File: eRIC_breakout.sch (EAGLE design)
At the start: 7 parts, among them U1 ERIC

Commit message: v1.6 ordered 4/18/2015
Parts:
- H1, H2: value M121X12_NO_SILK_KIT -> (none); device SparkFun-Connectors:M121X12_NO_SILK_KIT -> adafruit:PINHD-1X12-CB
- renumbered U1 to IC1
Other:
- moved on the sheet: H1, H2

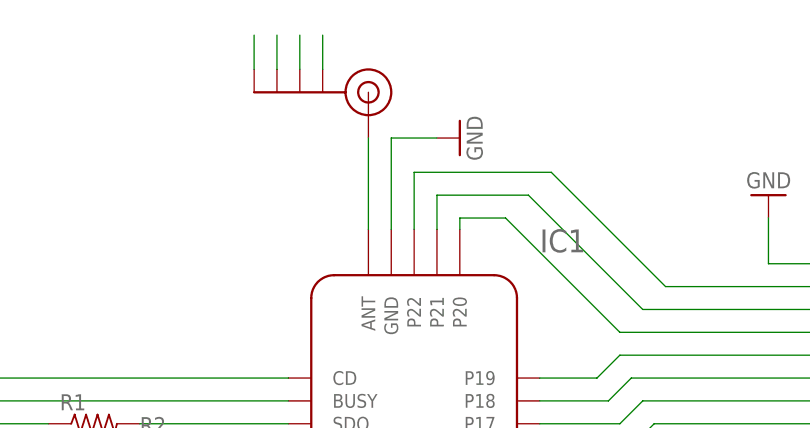
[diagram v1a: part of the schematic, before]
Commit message: SMA GND schematic changes and IC name added
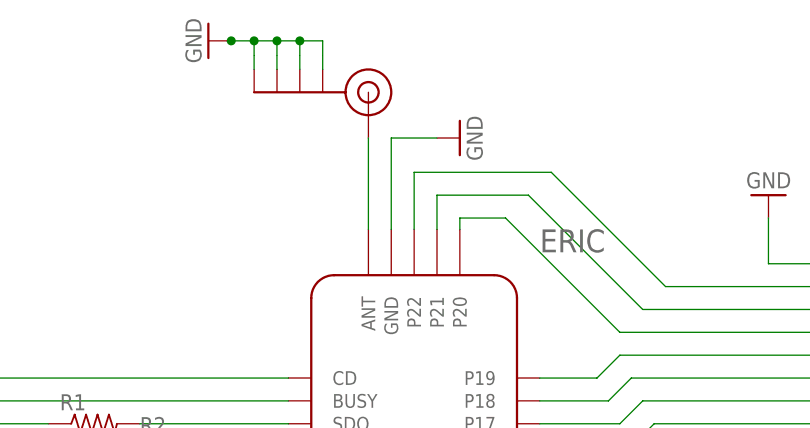
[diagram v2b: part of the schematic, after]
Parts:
- renumbered IC1 to ERIC
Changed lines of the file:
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@@
 </classes>
 <parts>
-<part name="IC1" library="lprs" deviceset="ERIC" device=""/>
+<part name="ERIC" library="lprs" deviceset="ERIC" device=""/>
 <part name="H2" library="adafruit" deviceset="PINHD-1X12" device="-CB"/>
 <part name="H1" library="adafruit" deviceset="PINHD-1X12" device="-CB"/>
@@
 <part name="J$1" library="SparkFun-Connectors" deviceset="SMA_EDGE" device=""/>
 <part name="GND1" library="supply1" deviceset="GND" device=""/>
+<part name="GND4" library="supply1" deviceset="GND" device=""/>
 </parts>
 <sheets>
@@
 </plain>
 <instances>
-<instance part="IC1" gate="G$1" x="38.1" y="34.29"/>
+<instance part="ERIC" gate="G$1" x="38.1" y="34.29"/>
 <instance part="H2" gate="G$1" x="105.41" y="55.88"/>
 <instance part="H1" gate="G$1" x="-5.08" y="43.18" rot="MR0"/>
@@
 <instance part="J$1" gate="1" x="46.99" y="87.63" rot="R270"/>
 <instance part="GND1" gate="1" x="91.44" y="76.2" rot="R180"/>
+<instance part="GND4" gate="1" x="29.21" y="93.345" rot="R270"/>
 </instances>
 <busses>
@@
 <segment>
 <pinref part="H1" gate="G$1" pin="1"/>
-<pinref part="IC1" gate="G$1" pin="CD"/>
+<pinref part="ERIC" gate="G$1" pin="CD"/>
 <wire x1="-2.54" y1="55.88" x2="38.1" y2="55.88" width="0.1524" layer="91"/>
 </segment>
@@
 <segment>
 <pinref part="H1" gate="G$1" pin="2"/>
-<pinref part="IC1" gate="G$1" pin="BUSY"/>
+<pinref part="ERIC" gate="G$1" pin="BUSY"/>
 <wire x1="-2.54" y1="53.34" x2="38.1" y2="53.34" width="0.1524" layer="91"/>
 </segment>
@@
 <segment>
 <pinref part="J$1" gate="1" pin="SIGNAL"/>
-<pinref part="IC1" gate="G$1" pin="ANT"/>
+<pinref part="ERIC" gate="G$1" pin="ANT"/>
 <wire x1="46.99" y1="82.55" x2="46.99" y2="72.39" width="0.1524" layer="91"/>
 </segment>
@@
 <segment>
 <pinref part="R1" gate="G$1" pin="2"/>
-<pinref part="IC1" gate="G$1" pin="SDO"/>
+<pinref part="ERIC" gate="G$1" pin="SDO"/>
 <wire x1="21.59" y1="50.8" x2="38.1" y2="50.8" width="0.1524" layer="91"/>
 </segment>
@@
 </segment>
 <segment>
-<pinref part="IC1" gate="G$1" pin="SDI"/>
+<pinref part="ERIC" gate="G$1" pin="SDI"/>
 <pinref part="R2" gate="G$1" pin="2"/>
 <wire x1="38.1" y1="48.26" x2="30.48" y2="48.26" width="0.1524" layer="91"/>
@@
 <segment>
 <pinref part="H1" gate="G$1" pin="5"/>
-<pinref part="IC1" gate="G$1" pin="HR"/>
+<pinref part="ERIC" gate="G$1" pin="HR"/>
 <wire x1="-2.54" y1="45.72" x2="38.1" y2="45.72" width="0.1524" layer="91"/>
 </segment>
@@
 <segment>
 <pinref part="H1" gate="G$1" pin="6"/>
-<pinref part="IC1" gate="G$1" pin="VCC"/>
+<pinref part="ERIC" gate="G$1" pin="VCC"/>
 <wire x1="-2.54" y1="43.18" x2="24.13" y2="43.18" width="0.1524" layer="91"/>
 <pinref part="C1" gate="G$1" pin="2"/>
@@
 <segment>
 <pinref part="H1" gate="G$1" pin="8"/>
-<pinref part="IC1" gate="G$1" pin="P8"/>
+<pinref part="ERIC" gate="G$1" pin="P8"/>
 <wire x1="-2.54" y1="38.1" x2="12.7" y2="38.1" width="0.1524" layer="91"/>
 <wire x1="12.7" y1="38.1" x2="29.21" y2="21.59" width="0.1524" layer="91"/>
@@
 <net name="N$12" class="0">
 <segment>
-<pinref part="IC1" gate="G$1" pin="RST"/>
+<pinref part="ERIC" gate="G$1" pin="RST"/>
 <pinref part="H1" gate="G$1" pin="9"/>
 <wire x1="49.53" y1="24.13" x2="49.53" y2="19.05" width="0.1524" layer="91"/>
@@
 <segment>
 <pinref part="H1" gate="G$1" pin="10"/>
-<pinref part="IC1" gate="G$1" pin="P10"/>
+<pinref part="ERIC" gate="G$1" pin="P10"/>
 <wire x1="-2.54" y1="33.02" x2="12.7" y2="33.02" width="0.1524" layer="91"/>
 <wire x1="12.7" y1="33.02" x2="29.21" y2="16.51" width="0.1524" layer="91"/>
@@
 <net name="N$14" class="0">
 <segment>
-<pinref part="IC1" gate="G$1" pin="P11"/>
+<pinref part="ERIC" gate="G$1" pin="P11"/>
 <pinref part="H1" gate="G$1" pin="11"/>
 <wire x1="54.61" y1="24.13" x2="54.61" y2="13.97" width="0.1524" layer="91"/>
@@
 <segment>
 <pinref part="H1" gate="G$1" pin="12"/>
-<pinref part="IC1" gate="G$1" pin="P12"/>
+<pinref part="ERIC" gate="G$1" pin="P12"/>
 <wire x1="-2.54" y1="27.94" x2="12.7" y2="27.94" width="0.1524" layer="91"/>
 <wire x1="12.7" y1="27.94" x2="29.21" y2="11.43" width="0.1524" layer="91"/>
@@
 <segment>
 <pinref part="GND2" gate="1" pin="GND"/>
-<pinref part="IC1" gate="G$1" pin="GND@2"/>
+<pinref part="ERIC" gate="G$1" pin="GND@2"/>
 <wire x1="54.61" y1="82.55" x2="49.53" y2="82.55" width="0.1524" layer="91"/>
 <wire x1="49.53" y1="82.55" x2="49.53" y2="72.39" width="0.1524" layer="91"/>
@@
 <segment>
 <pinref part="C1" gate="G$1" pin="1"/>
-<pinref part="IC1" gate="G$1" pin="GND@1"/>
+<pinref part="ERIC" gate="G$1" pin="GND@1"/>
 <wire x1="24.13" y1="35.56" x2="27.94" y2="35.56" width="0.1524" layer="91"/>
 <wire x1="27.94" y1="35.56" x2="33.02" y2="40.64" width="0.1524" layer="91"/>
@@
 <segment>
 <pinref part="J$1" gate="1" pin="GND@3"/>
-<wire x1="34.29" y1="90.17" x2="34.29" y2="93.98" width="0.1524" layer="91"/>
+<wire x1="34.29" y1="90.17" x2="34.29" y2="91.694" width="0.1524" layer="91"/>
 </segment>
 <segment>
 <pinref part="J$1" gate="1" pin="GND@2"/>
-<wire x1="36.83" y1="90.17" x2="36.83" y2="93.98" width="0.1524" layer="91"/>
+<wire x1="36.83" y1="90.17" x2="36.83" y2="91.694" width="0.1524" layer="91"/>
 </segment>
 <segment>
 <pinref part="J$1" gate="1" pin="GND@1"/>
-<wire x1="39.37" y1="90.17" x2="39.37" y2="93.98" width="0.1524" layer="91"/>
+<wire x1="39.37" y1="90.17" x2="39.37" y2="91.694" width="0.1524" layer="91"/>
 </segment>
 <segment>
 <pinref part="J$1" gate="1" pin="GND@0"/>
-<wire x1="41.91" y1="90.17" x2="41.91" y2="93.98" width="0.1524" layer="91"/>
+<wire x1="41.91" y1="90.17" x2="41.91" y2="91.694" width="0.1524" layer="91"/>
+</segment>
+<segment>
+<wire x1="34.29" y1="91.7575" x2="34.29" y2="93.345" width="0.1524" layer="91"/>
+<wire x1="34.29" y1="93.345" x2="31.75" y2="93.345" width="0.1524" layer="91"/>
+<wire x1="31.75" y1="93.345" x2="31.623" y2="93.345" width="0.1524" layer="91"/>
+<wire x1="36.83" y1="91.7575" x2="36.83" y2="93.345" width="0.1524" layer="91"/>
+<wire x1="36.83" y1="93.345" x2="34.29" y2="93.345" width="0.1524" layer="91"/>
+<junction x="34.29" y="93.345"/>
+<wire x1="39.37" y1="91.7575" x2="39.37" y2="93.345" width="0.1524" layer="91"/>
+<wire x1="39.37" y1="93.345" x2="36.83" y2="93.345" width="0.1524" layer="91"/>
+<junction x="36.83" y="93.345"/>
+<wire x1="41.91" y1="91.7575" x2="41.91" y2="93.345" width="0.1524" layer="91"/>
+<wire x1="41.91" y1="93.345" x2="39.37" y2="93.345" width="0.1524" layer="91"/>
+<junction x="39.37" y="93.345"/>
+<pinref part="GND4" gate="1" pin="GND"/>
+<junction x="31.75" y="93.345"/>
 </segment>
 </net>
 <net name="N$24" class="0">
 <segment>
-<pinref part="IC1" gate="G$1" pin="FS"/>
+<pinref part="ERIC" gate="G$1" pin="FS"/>
 <pinref part="H2" gate="G$1" pin="11"/>
 <wire x1="66.04" y1="43.18" x2="102.87" y2="43.18" width="0.1524" layer="91"/>
@@
 <net name="N$25" class="0">
 <segment>
-<pinref part="IC1" gate="G$1" pin="P13"/>
+<pinref part="ERIC" gate="G$1" pin="P13"/>
 <pinref part="H2" gate="G$1" pin="10"/>
 <wire x1="66.04" y1="40.64" x2="85.09" y2="40.64" width="0.1524" layer="91"/>
@@
 <net name="N$16" class="0">
 <segment>
-<pinref part="IC1" gate="G$1" pin="P15"/>
+<pinref part="ERIC" gate="G$1" pin="P15"/>
 <pinref part="H2" gate="G$1" pin="9"/>
 <wire x1="66.04" y1="45.72" x2="77.47" y2="45.72" width="0.1524" layer="91"/>
@@
 <segment>
 <pinref part="H2" gate="G$1" pin="8"/>
-<pinref part="IC1" gate="G$1" pin="P16"/>
+<pinref part="ERIC" gate="G$1" pin="P16"/>
 <wire x1="102.87" y1="50.8" x2="78.74" y2="50.8" width="0.1524" layer="91"/>
 <wire x1="78.74" y1="50.8" x2="76.2" y2="48.26" width="0.1524" layer="91"/>
@@
 <net name="N$18" class="0">
 <segment>
-<pinref part="IC1" gate="G$1" pin="P17"/>
+<pinref part="ERIC" gate="G$1" pin="P17"/>
 <pinref part="H2" gate="G$1" pin="7"/>
 <wire x1="66.04" y1="50.8" x2="74.93" y2="50.8" width="0.1524" layer="91"/>
@@
 <segment>
 <pinref part="H2" gate="G$1" pin="6"/>
-<pinref part="IC1" gate="G$1" pin="P18"/>
+<pinref part="ERIC" gate="G$1" pin="P18"/>
 <wire x1="102.87" y1="55.88" x2="76.2" y2="55.88" width="0.1524" layer="91"/>
 <wire x1="76.2" y1="55.88" x2="73.66" y2="53.34" width="0.1524" layer="91"/>
@@
 <net name="N$20" class="0">
 <segment>
-<pinref part="IC1" gate="G$1" pin="P19"/>
+<pinref part="ERIC" gate="G$1" pin="P19"/>
 <pinref part="H2" gate="G$1" pin="5"/>
 <wire x1="66.04" y1="55.88" x2="72.39" y2="55.88" width="0.1524" layer="91"/>
@@
 <segment>
 <pinref part="H2" gate="G$1" pin="4"/>
-<pinref part="IC1" gate="G$1" pin="P20"/>
+<pinref part="ERIC" gate="G$1" pin="P20"/>
 <wire x1="102.87" y1="60.96" x2="74.93" y2="60.96" width="0.1524" layer="91"/>
 <wire x1="74.93" y1="60.96" x2="62.23" y2="73.66" width="0.1524" layer="91"/>
@@
 <net name="N$22" class="0">
 <segment>
-<pinref part="IC1" gate="G$1" pin="P21"/>
+<pinref part="ERIC" gate="G$1" pin="P21"/>
 <pinref part="H2" gate="G$1" pin="3"/>
 <wire x1="54.61" y1="72.39" x2="54.61" y2="76.2" width="0.1524" layer="91"/>
@@
 <net name="N$23" class="0">
 <segment>
-<pinref part="IC1" gate="G$1" pin="P22"/>
+<pinref part="ERIC" gate="G$1" pin="P22"/>
 <pinref part="H2" gate="G$1" pin="2"/>
 <wire x1="52.07" y1="72.39" x2="52.07" y2="78.74" width="0.1524" layer="91"/>

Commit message: component values
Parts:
- C1: value (none) -> .1uF
- R1, R2: value (none) -> 10K
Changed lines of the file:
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@@
 <setting verticaltext="up"/>
 </settings>
-<grid distance="0.0635" unitdist="mm" unit="mm" style="lines" multiple="1" display="yes" altdistance="0.0635" altunitdist="mm" altunit="mm"/>
+<grid distance="0.1" unitdist="inch" unit="inch" style="lines" multiple="1" display="no" altdistance="0.01" altunitdist="inch" altunit="inch"/>
 <layers>
 <layer number="1" name="Top" color="4" fill="1" visible="no" active="no"/>
@@
 <part name="H2" library="adafruit" deviceset="PINHD-1X12" device="-CB"/>
 <part name="H1" library="adafruit" deviceset="PINHD-1X12" device="-CB"/>
-<part name="R1" library="adafruit" deviceset="R-US_" device="R0603"/>
-<part name="R2" library="adafruit" deviceset="R-US_" device="R0603"/>
-<part name="C1" library="adafruit" deviceset="C-US" device="C0603K"/>
+<part name="R1" library="adafruit" deviceset="R-US_" device="R0603" value="10K"/>
+<part name="R2" library="adafruit" deviceset="R-US_" device="R0603" value="10K"/>
+<part name="C1" library="adafruit" deviceset="C-US" device="C0603K" value=".1uF"/>
 <part name="GND2" library="supply1" deviceset="GND" device=""/>
 <part name="GND3" library="supply1" deviceset="GND" device=""/>
